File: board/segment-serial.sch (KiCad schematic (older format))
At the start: 20 parts, among them J1 Conn_01x07_Female, Q1 2N3906, Q2 2N3906, Q3 2N3906, Q4 2N3906, U1 74HC164, U2 CA56-12EWA, U3 74HC164

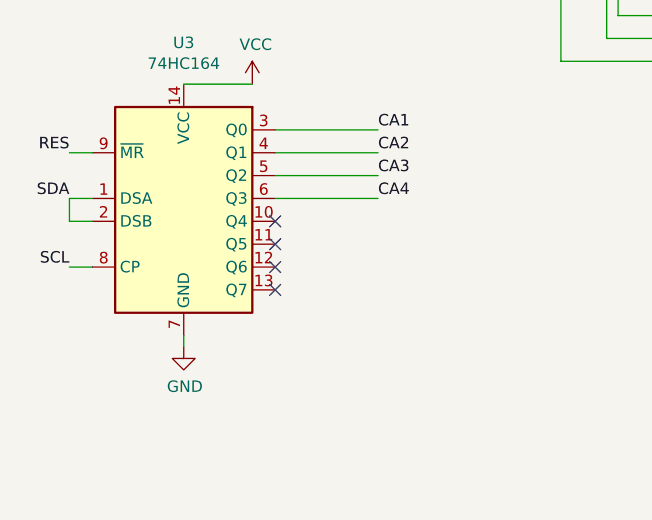
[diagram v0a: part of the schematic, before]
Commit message: Fixing issue with unconnected pins in U3
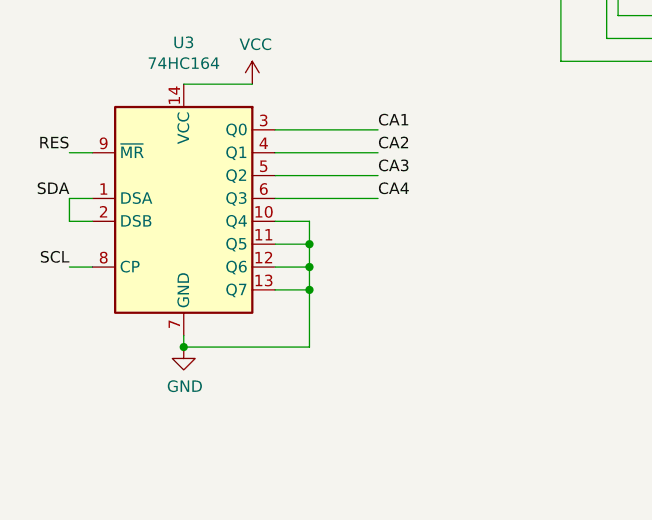
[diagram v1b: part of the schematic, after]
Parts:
- R1, R10, R11, R12, R2, R3, R4, R5, R6, R7, R8, R9: footprint Resistor_THT:R_Axial_DIN0207_L6.3mm_D2.5mm_P2.54mm_Vertical -> Resistor_THT:R_Axial_DIN0207_L6.3mm_D2.5mm_P7.62mm_Horizontal
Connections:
- net GND: now also U3.10 (Q4), U3.11 (Q5), U3.12 (Q6), U3.13 (Q7)
- no-connect marks 5 -> 1
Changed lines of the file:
@@
 F 0 "R10" V 6095 5800 50  0000 C CNN
 F 1 "1K" V 6186 5800 50  0000 C CNN
-F 2 "Resistor_THT:R_Axial_DIN0207_L6.3mm_D2.5mm_P2.54mm_Vertical" V 6340 5790 50  0001 C CNN
+F 2 "Resistor_THT:R_Axial_DIN0207_L6.3mm_D2.5mm_P7.62mm_Horizontal" V 6340 5790 50  0001 C CNN
 F 3 "~" H 6300 5800 50  0001 C CNN
 	1    6300 5800
@@
 F 0 "R11" V 7445 5250 50  0000 C CNN
 F 1 "1K" V 7536 5250 50  0000 C CNN
-F 2 "Resistor_THT:R_Axial_DIN0207_L6.3mm_D2.5mm_P2.54mm_Vertical" V 7690 5240 50  0001 C CNN
+F 2 "Resistor_THT:R_Axial_DIN0207_L6.3mm_D2.5mm_P7.62mm_Horizontal" V 7690 5240 50  0001 C CNN
 F 3 "~" H 7650 5250 50  0001 C CNN
 	1    7650 5250
@@
 F 0 "R12" V 7445 5800 50  0000 C CNN
 F 1 "1K" V 7536 5800 50  0000 C CNN
-F 2 "Resistor_THT:R_Axial_DIN0207_L6.3mm_D2.5mm_P2.54mm_Vertical" V 7690 5790 50  0001 C CNN
+F 2 "Resistor_THT:R_Axial_DIN0207_L6.3mm_D2.5mm_P7.62mm_Horizontal" V 7690 5790 50  0001 C CNN
 F 3 "~" H 7650 5800 50  0001 C CNN
 	1    7650 5800
@@
 F 0 "R9" V 6095 5250 50  0000 C CNN
 F 1 "1K" V 6186 5250 50  0000 C CNN
-F 2 "Resistor_THT:R_Axial_DIN0207_L6.3mm_D2.5mm_P2.54mm_Vertical" V 6340 5240 50  0001 C CNN
+F 2 "Resistor_THT:R_Axial_DIN0207_L6.3mm_D2.5mm_P7.62mm_Horizontal" V 6340 5240 50  0001 C CNN
 F 3 "~" H 6300 5250 50  0001 C CNN
 	1    6300 5250
@@
 F 0 "R4" H 4118 2696 50  0000 L CNN
 F 1 "330" H 4118 2605 50  0000 L CNN
-F 2 "Resistor_THT:R_Axial_DIN0207_L6.3mm_D2.5mm_P2.54mm_Vertical" V 4090 2640 50  0001 C CNN
+F 2 "Resistor_THT:R_Axial_DIN0207_L6.3mm_D2.5mm_P7.62mm_Horizontal" V 4090 2640 50  0001 C CNN
 F 3 "~" H 4050 2650 50  0001 C CNN
 	1    4050 2650
@@
 F 0 "R5" H 4418 2696 50  0000 L CNN
 F 1 "330" H 4418 2605 50  0000 L CNN
-F 2 "Resistor_THT:R_Axial_DIN0207_L6.3mm_D2.5mm_P2.54mm_Vertical" V 4390 2640 50  0001 C CNN
+F 2 "Resistor_THT:R_Axial_DIN0207_L6.3mm_D2.5mm_P7.62mm_Horizontal" V 4390 2640 50  0001 C CNN
 F 3 "~" H 4350 2650 50  0001 C CNN
 	1    4350 2650
@@
 F 0 "R6" H 4668 2696 50  0000 L CNN
 F 1 "330" H 4668 2605 50  0000 L CNN
-F 2 "Resistor_THT:R_Axial_DIN0207_L6.3mm_D2.5mm_P2.54mm_Vertical" V 4640 2640 50  0001 C CNN
+F 2 "Resistor_THT:R_Axial_DIN0207_L6.3mm_D2.5mm_P7.62mm_Horizontal" V 4640 2640 50  0001 C CNN
 F 3 "~" H 4600 2650 50  0001 C CNN
 	1    4600 2650
@@
 F 0 "R7" H 4918 2696 50  0000 L CNN
 F 1 "330" H 4918 2605 50  0000 L CNN
-F 2 "Resistor_THT:R_Axial_DIN0207_L6.3mm_D2.5mm_P2.54mm_Vertical" V 4890 2640 50  0001 C CNN
+F 2 "Resistor_THT:R_Axial_DIN0207_L6.3mm_D2.5mm_P7.62mm_Horizontal" V 4890 2640 50  0001 C CNN
 F 3 "~" H 4850 2650 50  0001 C CNN
 	1    4850 2650
@@
 F 0 "R8" H 5218 2696 50  0000 L CNN
 F 1 "330" H 5218 2605 50  0000 L CNN
-F 2 "Resistor_THT:R_Axial_DIN0207_L6.3mm_D2.5mm_P2.54mm_Vertical" V 5190 2640 50  0001 C CNN
+F 2 "Resistor_THT:R_Axial_DIN0207_L6.3mm_D2.5mm_P7.62mm_Horizontal" V 5190 2640 50  0001 C CNN
 F 3 "~" H 5150 2650 50  0001 C CNN
 	1    5150 2650
@@
 F 0 "R3" H 3868 2696 50  0000 L CNN
 F 1 "330" H 3868 2605 50  0000 L CNN
-F 2 "Resistor_THT:R_Axial_DIN0207_L6.3mm_D2.5mm_P2.54mm_Vertical" V 3840 2640 50  0001 C CNN
+F 2 "Resistor_THT:R_Axial_DIN0207_L6.3mm_D2.5mm_P7.62mm_Horizontal" V 3840 2640 50  0001 C CNN
 F 3 "~" H 3800 2650 50  0001 C CNN
 	1    3800 2650
@@
 F 0 "R2" H 3432 2604 50  0000 R CNN
 F 1 "330" H 3432 2695 50  0000 R CNN
-F 2 "Resistor_THT:R_Axial_DIN0207_L6.3mm_D2.5mm_P2.54mm_Vertical" V 3540 2640 50  0001 C CNN
+F 2 "Resistor_THT:R_Axial_DIN0207_L6.3mm_D2.5mm_P7.62mm_Horizontal" V 3540 2640 50  0001 C CNN
 F 3 "~" H 3500 2650 50  0001 C CNN
 	1    3500 2650
@@
 F 0 "R1" H 3182 2604 50  0000 R CNN
 F 1 "330" H 3182 2695 50  0000 R CNN
-F 2 "Resistor_THT:R_Axial_DIN0207_L6.3mm_D2.5mm_P2.54mm_Vertical" V 3290 2640 50  0001 C CNN
+F 2 "Resistor_THT:R_Axial_DIN0207_L6.3mm_D2.5mm_P7.62mm_Horizontal" V 3290 2640 50  0001 C CNN
 F 3 "~" H 3250 2650 50  0001 C CNN
 	1    3250 2650
@@
 Wire Wire Line
 	2000 5150 2450 5150
-NoConn ~ 2000 5250
-NoConn ~ 2000 5350
-NoConn ~ 2000 5450
-NoConn ~ 2000 5550
 $Comp
 L power:VCC #PWR03
@@
 	1050 3400 1050 3300
 NoConn ~ 3450 1450
+Wire Wire Line
+	2000 5250 2150 5250
+Wire Wire Line
+	2150 5250 2150 5350
+Wire Wire Line
+	2150 5800 1600 5800
+Connection ~ 1600 5800
+Wire Wire Line
+	2000 5350 2150 5350
+Connection ~ 2150 5350
+Wire Wire Line
+	2150 5350 2150 5450
+Wire Wire Line
+	2000 5450 2150 5450
+Connection ~ 2150 5450
+Wire Wire Line
+	2150 5450 2150 5550
+Wire Wire Line
+	2000 5550 2150 5550
+Connection ~ 2150 5550
+Wire Wire Line
+	2150 5550 2150 5800
 $EndSCHEMATC
